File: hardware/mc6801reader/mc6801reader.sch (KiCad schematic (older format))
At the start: 21 parts, among them J1 +5V PWR, J2 Serial port, SW1 SW_DPDT_x2, U1 MC6801, U2 74LS373, U3 GAL16V8, U4 2764, Y1 2.4576MHz

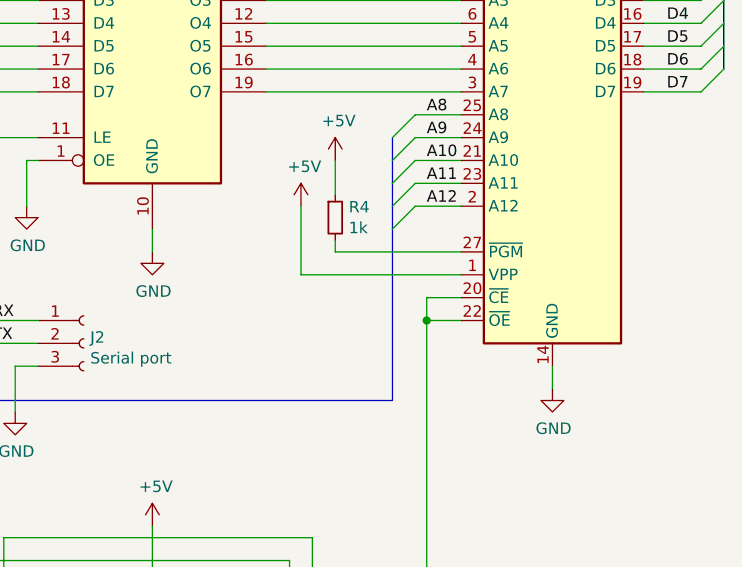
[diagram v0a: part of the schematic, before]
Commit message: A11 is grounded
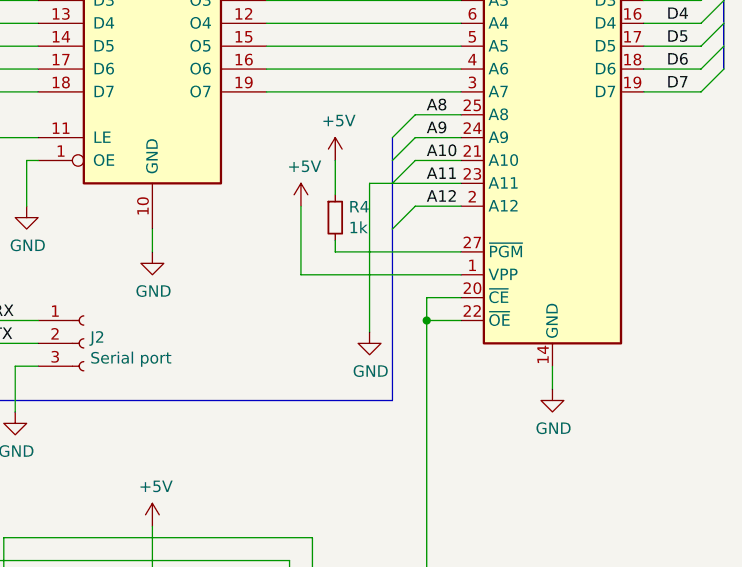
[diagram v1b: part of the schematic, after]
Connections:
- net A11 is gone; now on net GND: U1.26 (P43), U3.6 (I6), U4.23 (A11)
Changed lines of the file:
@@
 EESchema Schematic File Version 4
-LIBS:mc6801reader-cache
 EELAYER 26 0
 EELAYER END
@@
 	6750 2800 6850 2700
 Entry Wire Line
-	6750 2900 6850 2800
-Entry Wire Line
-	6750 3000 6850 2900
-Entry Wire Line
 	6750 3100 6850 3000
 Wire Wire Line
@@
 Wire Wire Line
 	6850 2700 7050 2700
-Wire Wire Line
-	6850 2800 7050 2800
-Wire Wire Line
-	6850 2900 7050 2900
 Wire Wire Line
 	6850 3000 7050 3000
@@
 NoConn ~ 2900 2400
 NoConn ~ 2900 2500
-Wire Bus Line
-	4450 1250 4450 2400
 Wire Wire Line
 	6300 4550 6300 4800
@@
 Wire Wire Line
 	6400 4900 6200 4900
-Wire Wire Line
-	3900 2500 5200 2500
-Wire Wire Line
-	3900 1800 5200 1800
-Wire Wire Line
-	3900 1900 5200 1900
-Wire Wire Line
-	3900 2000 5200 2000
-Wire Wire Line
-	3900 2100 5200 2100
-Wire Wire Line
-	3900 2200 5200 2200
-Wire Wire Line
-	3900 2300 5200 2300
-Wire Wire Line
-	3900 2400 5200 2400
-Wire Bus Line
-	6750 2700 6750 3850
-Wire Bus Line
-	4900 3850 4900 5200
-Wire Bus Line
-	8200 1250 8200 2400
-Wire Bus Line
-	4450 2800 4450 3850
 Text Label 5000 3500 0    50   ~ 0
 RX
 Text Label 5000 3600 0    50   ~ 0
 TX
+Wire Bus Line
+	4450 1250 4450 2400
+Wire Wire Line
+	6850 2800 7050 2800
+Entry Wire Line
+	6750 2900 6850 2800
+$Comp
+L power:GND #PWR?
+U 1 1 5D7B80EE
+P 6650 3550
+F 0 "#PWR?" H 6650 3300 50  0001 C CNN
+F 1 "GND" H 6655 3377 50  0000 C CNN
+F 2 "" H 6650 3550 50  0001 C CNN
+F 3 "" H 6650 3550 50  0001 C CNN
+	1    6650 3550
+	1    0    0    -1
+$EndComp
+Wire Wire Line
+	6650 2900 6650 3550
+Wire Wire Line
+	3900 2400 5200 2400
+Wire Wire Line
+	3900 2300 5200 2300
+Wire Wire Line
+	3900 2200 5200 2200
+Wire Wire Line
+	3900 2100 5200 2100
+Wire Wire Line
+	3900 2000 5200 2000
+Wire Wire Line
+	3900 1900 5200 1900
+Wire Wire Line
+	3900 1800 5200 1800
+Wire Wire Line
+	3900 2500 5200 2500
+Wire Wire Line
+	6650 2900 7050 2900
+Wire Bus Line
+	4900 3850 4900 5200
+Wire Bus Line
+	6750 2700 6750 3850
+Wire Bus Line
+	4450 2800 4450 3850
+Wire Bus Line
+	8200 1250 8200 2400
 $EndSCHEMATC
